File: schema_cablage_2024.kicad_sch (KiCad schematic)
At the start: 60 parts, among them M1 REV_NEO_Brushless_Motor, M2 REV_NEO_Brushless_Motor, M3 am-3775a, M4 am-3775a, M5 am-3775a, M6 REV_NEO_Brushless_Motor, M7 REV_NEO_Brushless_Motor, M8 REV_NEO_Brushless_Motor, M9 REV_NEO_Brushless_Motor, P1 SB-50, P2 SB-50, U1 REV_Spark_MAX, U10 CTRE_SRX_Mag_Encoder, U11 VEX_CTRE_Talon_SRX, U12 REV_Spark_MAX, U13 REV_Spark_MAX, U14 REV_Spark_MAX, U15 REV_Spark_MAX, U16 CTRE_SRX_Mag_Encoder, U2 REV_Spark_MAX, U3 Banner_Photoelectric_Sensor_Q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, U4 Banner_Photoelectric_Sensor_Q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, U5 RoboRIO, U6 VEX_CTRE_Talon_SRX, U7 VEX_CTRE_Talon_SRX, U8 Kauai_navX2-MXP, U9 CTRE_SRX_Mag_Encoder

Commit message: Ajout Limelight + webcam
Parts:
- added F11: 10A, symbol Device:Fuse_Small
- added U5: Webcam_HD_Lifecam_3000, symbol FRC_Components:Webcam_HD_Lifecam_3000
- added U7: Limelight 3, symbol FRC_Components:Limelight
- renumbered U8 to U10, U9 to U11, U10 to U12, U11 to U13, U12 to U14, U13 to U15, U14 to U16, U15 to U17, U16 to U18, U5 to U6, U6 to U8, U7 to U9
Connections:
- net ETH: now also U7. (V-)
- net V+: now also U7. (V-)
- net V-: now also U7. (V-)
- new net: M9. (IN_C), U17. (VIN-)
- new net: M1. (IN_C), U1. (VIN-)
- new net: M8. (IN_C), U16. (VIN-)
- new net: M6. (IN_C), U14. (VIN-)
- new net: M2. (IN_C), U2. (VIN-)
- new net: F11.1, PS1. (VOUT9)
- new net: F11.2, PS1. (VOUT9)
- new net: M7. (IN_C), U15. (VIN-)
- new net Sous-système vision/ETH_A: GN1. (GND)
- new net Sous-système vision/ETH_B: GN1. (GND)
- new net USB: U5. (USB), U6. (~{SPI_CS3})
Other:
- moved on the sheet: D1, D2, D3, D4, DS1, GN1, U10, U3, U4, U6, VR2

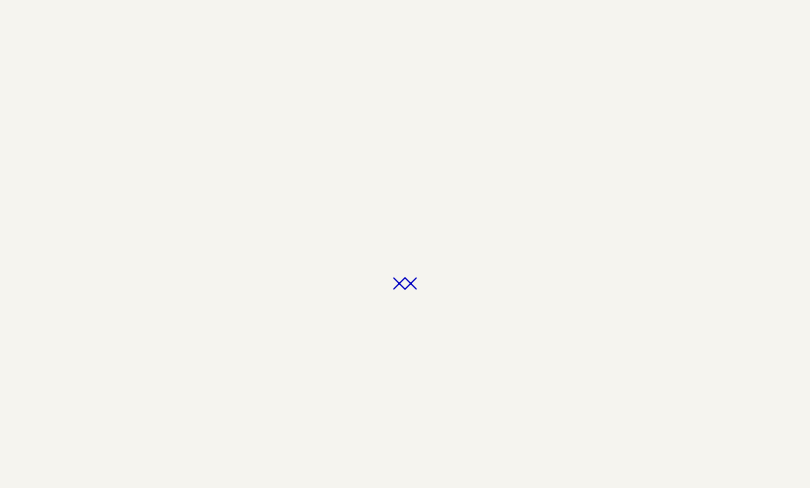
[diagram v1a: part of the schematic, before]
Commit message: Remove rogue no-connects, update to KiCad 8.0
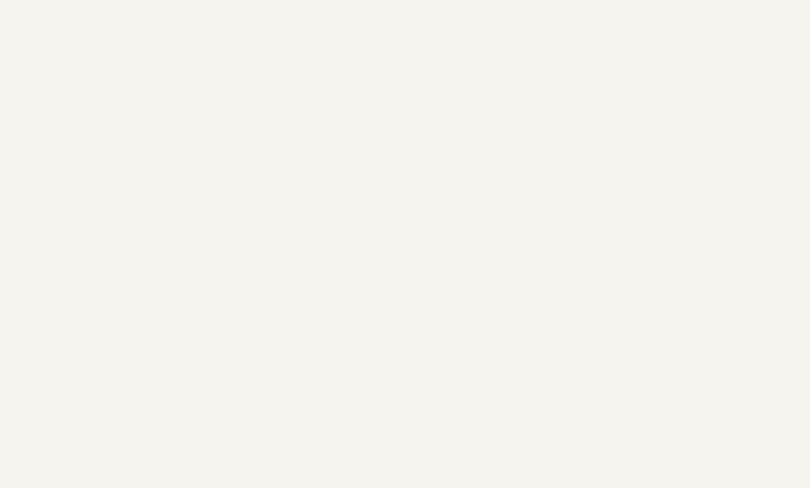
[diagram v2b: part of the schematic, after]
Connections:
- new net: M9. (IN_C), U17. (VIN-)
- new net: M1. (IN_C), U1. (VIN-)
- new net: M8. (IN_C), U16. (VIN-)
- new net: M6. (IN_C), U14. (VIN-)
- new net: M2. (IN_C), U2. (VIN-)
- new net: M7. (IN_C), U15. (VIN-)
- no-connect marks 167 -> 165

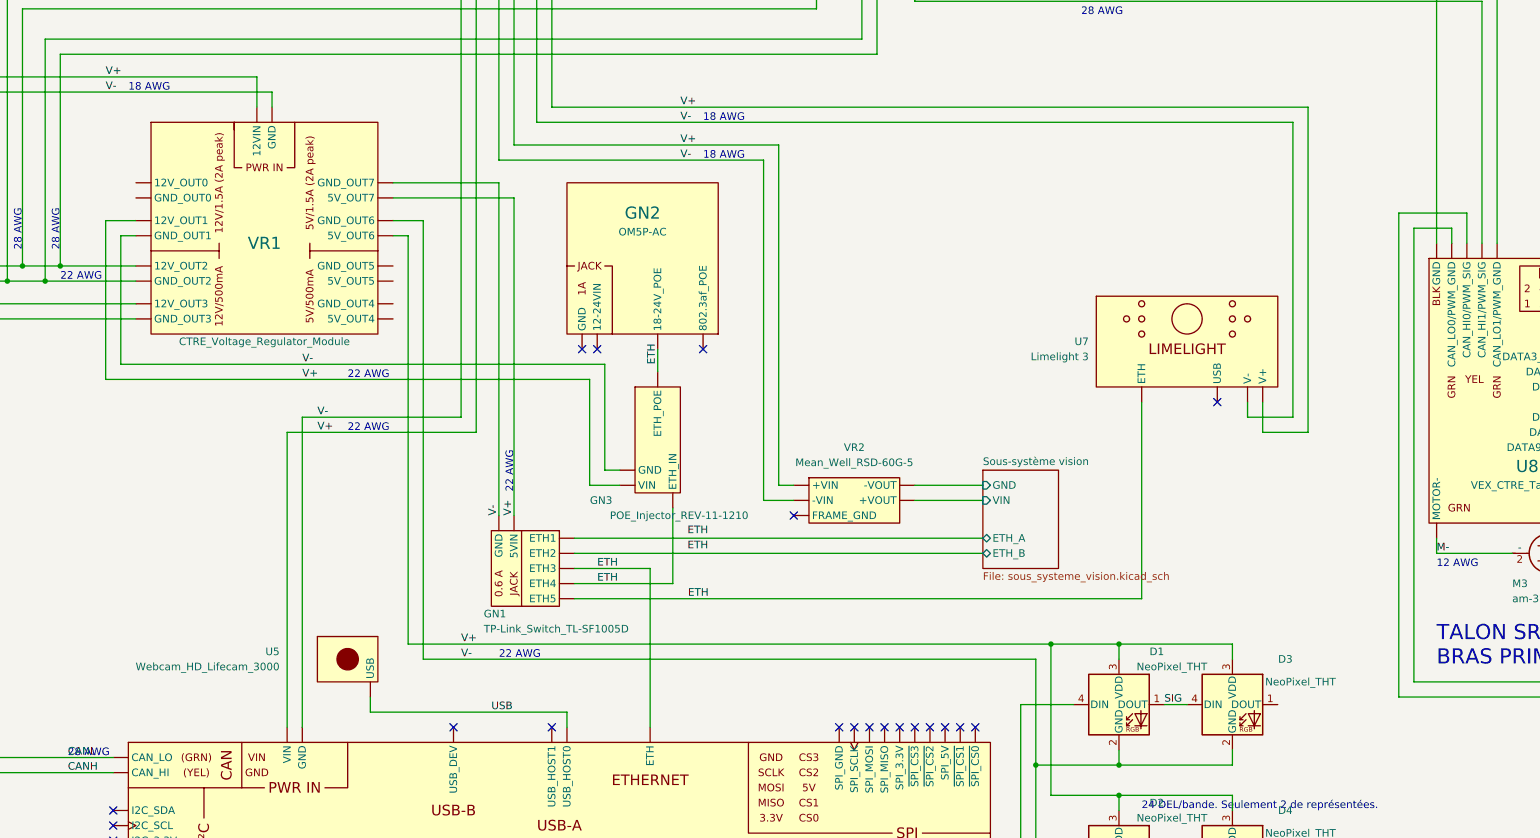
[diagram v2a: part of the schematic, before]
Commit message: Added Coral
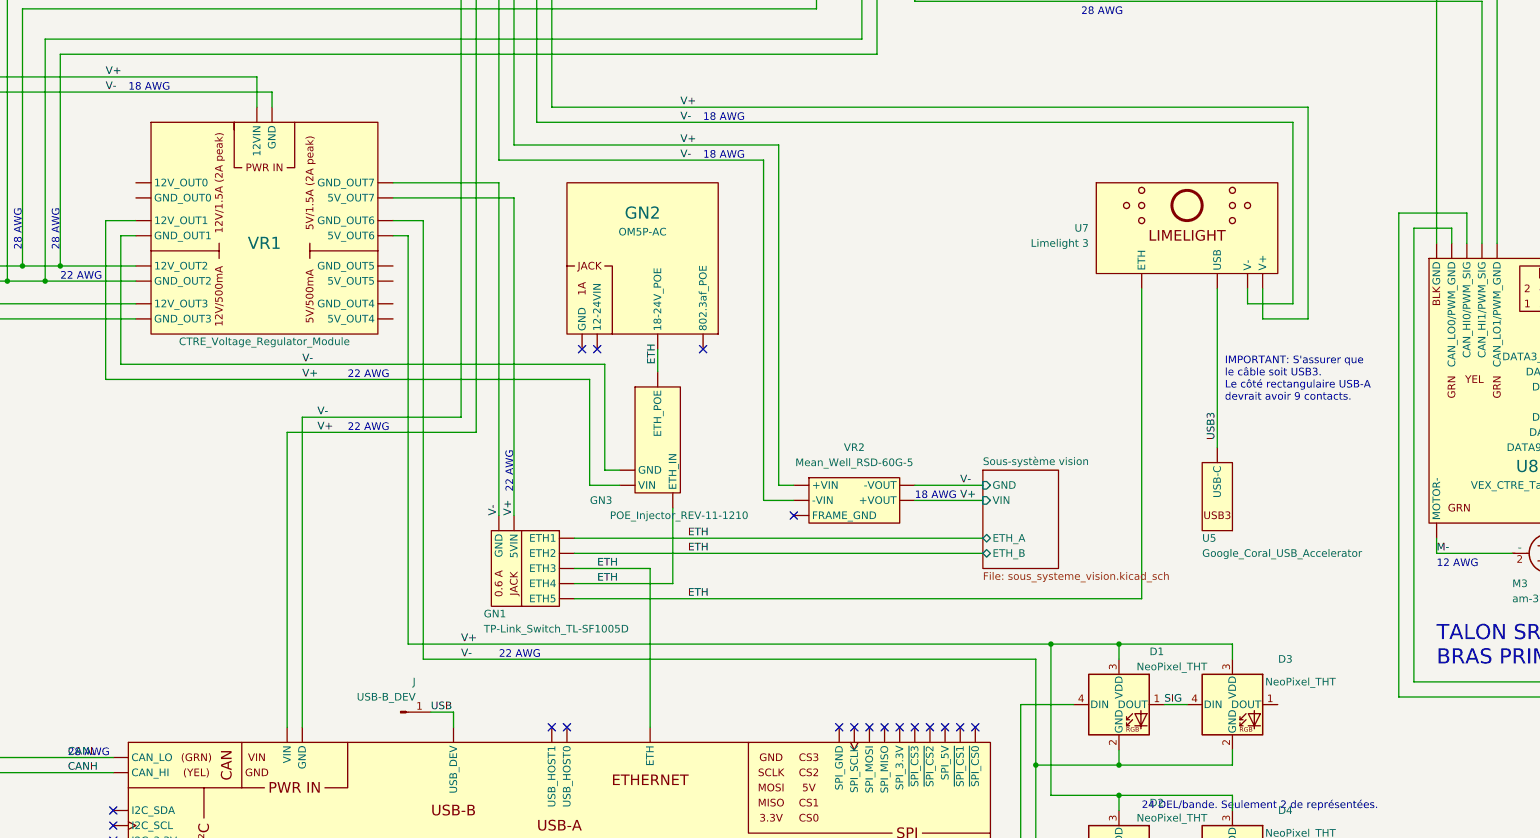
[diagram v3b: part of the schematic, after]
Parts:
- removed U5: Webcam_HD_Lifecam_3000, symbol FRC_Components:Webcam_HD_Lifecam_3000
- added J: USB-B_DEV, symbol Connector:Conn_01x01_Pin
- added U5: Google_Coral_USB_Accelerator, symbol FRC_Components:Google_Coral_USB_Accelerator
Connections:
- net Sous-système vision/ETH_A is gone; now on net V-: GN1. (GND)
- net Sous-système vision/ETH_B is gone; now on net V-: GN1. (GND)
- net Sous-système vision/GND is gone; now on net V-: VR2. (FRAME_GND)
- net Sous-système vision/VIN is gone; now on net V-: VR2. (FRAME_GND)
- net USB: now also J.1 (Pin_1)
- new net: M9. (IN_C), U17. (VIN-)
- new net: M1. (IN_C), U1. (VIN-)
- new net: M8. (IN_C), U16. (VIN-)
- new net: M6. (IN_C), U14. (VIN-)
- new net: M2. (IN_C), U2. (VIN-)
- new net: M7. (IN_C), U15. (VIN-)
- new net USB3: U5. (USB-C), U7. (V-)
- no-connect marks 165 -> 164
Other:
- note added: "IMPORTANT: S'assurer que le câble soit USB3. Le côté rectangulaire USB-A devrait avoir 9 contacts."
- moved on the sheet: U7

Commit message: Corrections coquilles
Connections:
- new net: M9. (IN_C), U17. (VIN-)
- new net: M1. (IN_C), U1. (VIN-)
- new net: M8. (IN_C), U16. (VIN-)
- new net: M6. (IN_C), U14. (VIN-)
- new net: M2. (IN_C), U2. (VIN-)
- new net: M7. (IN_C), U15. (VIN-)
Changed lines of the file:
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@@
 	(wire
 		(pts
-			(xy 200.66 180.34) (xy 200.66 205.74)
+			(xy 203.2 180.34) (xy 203.2 205.74)
 		)
 		(stroke
@@
 	(wire
 		(pts
-			(xy 254 180.34) (xy 200.66 180.34)
+			(xy 254 180.34) (xy 203.2 180.34)
 		)
 		(stroke
@@
 	(wire
 		(pts
-			(xy 200.66 205.74) (xy 181.61 205.74)
+			(xy 203.2 205.74) (xy 181.61 205.74)
 		)
 		(stroke
@@
 	(text "24 DEL/bande. Seulement 2 de représentées."
 		(exclude_from_sim no)
-		(at 469.9 392.43 0)
+		(at 464.058 388.112 0)
 		(effects
 			(font
@@
 	(text "28 AWG"
 		(exclude_from_sim no)
-		(at 289.56 383.54 0)
+		(at 281.686 383.54 0)
 		(effects
 			(font
@@
 	)
 	(symbol
-		(lib_name "FRC_Components:REV_Spark_MAX")
 		(lib_id "FRC_Components:REV_Spark_MAX")
 		(at 711.2 364.49 90)
@@
 	)
 	(symbol
-		(lib_name "FRC_Components:CTRE_SRX_Mag_Encoder")
 		(lib_id "FRC_Components:CTRE_SRX_Mag_Encoder")
 		(at 655.32 93.98 270)
@@
 	)
 	(symbol
-		(lib_name "FRC_Components:REV_Spark_MAX")
 		(lib_id "FRC_Components:REV_Spark_MAX")
 		(at 160.02 157.48 270)
@@
 	)
 	(symbol
-		(lib_name "FRC_Components:REV_NEO_Brushless_Motor")
 		(lib_id "FRC_Components:REV_NEO_Brushless_Motor")
 		(at 737.87 364.49 90)
@@
 	)
 	(symbol
-		(lib_name "FRC_Components:REV_Spark_MAX")
 		(lib_id "FRC_Components:REV_Spark_MAX")
 		(at 711.2 330.2 90)
@@
 	)
 	(symbol
-		(lib_name "FRC_Components:VEX_CTRE_Talon_SRX")
 		(lib_id "FRC_Components:VEX_CTRE_Talon_SRX")
 		(at 547.37 88.9 0)
@@
 	)
 	(symbol
-		(lib_name "FRC_Components:CTRE_SRX_Mag_Encoder")
 		(lib_id "FRC_Components:CTRE_SRX_Mag_Encoder")
 		(at 762 93.98 270)
@@
 	)
 	(symbol
-		(lib_name "FRC_Components:CTRE_SRX_Mag_Encoder")
 		(lib_id "FRC_Components:CTRE_SRX_Mag_Encoder")
 		(at 604.52 322.58 270)
@@
 	)
 	(symbol
-		(lib_name "FRC_Components:REV_NEO_Brushless_Motor")
 		(lib_id "FRC_Components:REV_NEO_Brushless_Motor")
 		(at 737.87 330.2 90)
@@
 	)
 	(symbol
-		(lib_name "FRC_Components:REV_NEO_Brushless_Motor")
 		(lib_id "FRC_Components:REV_NEO_Brushless_Motor")
 		(at 737.87 231.14 90)
@@
 	)
 	(symbol
-		(lib_name "FRC_Components:REV_NEO_Brushless_Motor")
 		(lib_id "FRC_Components:REV_NEO_Brushless_Motor")
 		(at 133.35 191.77 270)
@@
 	)
 	(symbol
-		(lib_name "FRC_Components:REV_Spark_MAX")
 		(lib_id "FRC_Components:REV_Spark_MAX")
 		(at 160.02 191.77 270)
@@
 	)
 	(symbol
-		(lib_name "FRC_Components:VEX_CTRE_Talon_SRX")
 		(lib_id "FRC_Components:VEX_CTRE_Talon_SRX")
 		(at 534.67 317.5 0)
@@
 	)
 	(symbol
-		(lib_name "FRC_Components:REV_NEO_Brushless_Motor")
 		(lib_id "FRC_Components:REV_NEO_Brushless_Motor")
 		(at 133.35 157.48 270)
@@
 	)
 	(symbol
-		(lib_name "FRC_Components:Banner_Photoelectric_Sensor_QS18VN6LP")
 		(lib_id "FRC_Components:Banner_Photoelectric_Sensor_QS18VN6LP")
 		(at 223.52 440.69 90)
@@
 	)
 	(symbol
-		(lib_name "FRC_Components:Banner_Photoelectric_Sensor_QS18VN6LP")
 		(lib_id "FRC_Components:Banner_Photoelectric_Sensor_QS18VN6LP")
 		(at 223.52 421.64 90)
@@
 	)
 	(symbol
-		(lib_name "FRC_Components:VEX_CTRE_Talon_SRX")
 		(lib_id "FRC_Components:VEX_CTRE_Talon_SRX")
 		(at 692.15 88.9 0)
@@
 	)
 	(symbol
-		(lib_name "FRC_Components:REV_Spark_MAX")
 		(lib_id "FRC_Components:REV_Spark_MAX")
 		(at 711.2 231.14 90)
@@
 	)
 	(symbol
-		(lib_name "FRC_Components:REV_NEO_Brushless_Motor")
 		(lib_id "FRC_Components:REV_NEO_Brushless_Motor")
 		(at 737.87 265.43 90)
@@
 	)
 	(symbol
-		(lib_name "FRC_Components:REV_Spark_MAX")
 		(lib_id "FRC_Components:REV_Spark_MAX")
 		(at 711.2 265.43 90)
